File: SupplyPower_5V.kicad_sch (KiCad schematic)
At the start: 3 parts, among them U1 K7805-1000R3

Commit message: Развел все
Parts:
- removed U1: K7805-1000R3, K78xx-1000R3, symbol DCDC_My:K78xx-1000R3
- added D51: +5V, LED_SMD:LED_0805_2012Metric_Pad1.15x1.40mm_HandSolder, symbol Device:LED_Small
- added R97: 500, Resistor_SMD:R_0805_2012Metric_Pad1.20x1.40mm_HandSolder, symbol Device:R_Small
- added U1: K78xxM-1000R3, DCDC_My:K78xxM-1000R3, symbol DCDC_My:K78xxM-1000R3
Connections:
- net +15V: now also U1.1 (Vin)
- net +5V: now also R97.2, U1.3 (+Vo)
- net GND: now also D51.1 (K), U1.2 (GND)
- new net: D51.2 (A), R97.1

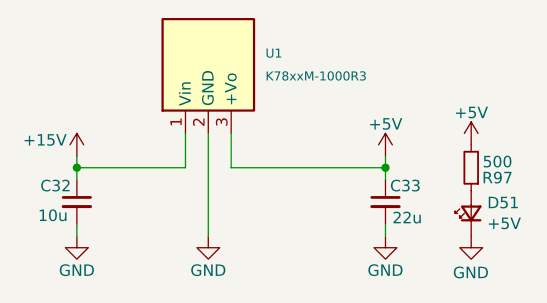
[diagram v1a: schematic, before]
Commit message: Отправил на проверку в резонит: изменил BOM
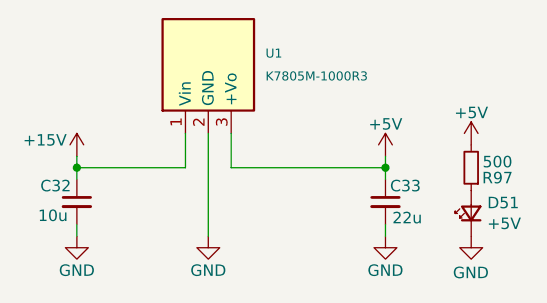
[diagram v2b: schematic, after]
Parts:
- U1: value K78xxM-1000R3 -> K7805M-1000R3
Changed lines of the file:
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@@
 			)
 		)
-		(property "Description" ""
+		(property "Description" "KP-2012SYC"
 			(at 165.1 102.235 0)
 			(effects
@@
 			)
 		)
-		(property "Value" "K78xxM-1000R3"
+		(property "Value" "K7805M-1000R3"
 			(at 142.24 86.995 90)
 			(effects

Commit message: Исправления: исправил нумерацию ножек датчиков тока
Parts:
- U1: footprint DCDC_My:K78xxM-1000R3 -> K78xxM-1000R3
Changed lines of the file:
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@@
 			)
 		)
-		(property "Description" ""
+		(property "Description" "Unpolarized capacitor, small symbol"
 			(at 155.575 100.965 0)
 			(effects
@@
 	)
 	(symbol
-		(lib_name "GND_2")
 		(lib_id "power:GND")
 		(at 121.285 104.775 0)
@@
 			)
 		)
-		(property "Description" ""
+		(property "Description" "Power symbol creates a global label with name \"GND\" , ground"
 			(at 121.285 104.775 0)
 			(effects
@@
 			)
 		)
-		(property "Description" ""
+		(property "Description" "Power symbol creates a global label with name \"GND\" , ground"
 			(at 135.89 104.775 0)
 			(effects
@@
 			)
 		)
-		(property "Description" ""
+		(property "Description" "Unpolarized capacitor, small symbol"
 			(at 121.285 100.965 0)
 			(effects
@@
 			)
 		)
-		(property "Description" ""
+		(property "Description" "Power symbol creates a global label with name \"+15V\""
 			(at 121.285 95.885 0)
 			(effects
@@
 			)
 		)
-		(property "Description" "KP-2012SYC"
+		(property "Description" "Light emitting diode, small symbol"
 			(at 165.1 102.235 0)
 			(effects
@@
 			)
 		)
-		(property "Description" ""
+		(property "Description" "Resistor, small symbol"
 			(at 165.1 97.155 0)
 			(effects
@@
 	)
 	(symbol
-		(lib_name "GND_1")
 		(lib_id "power:GND")
 		(at 155.575 104.775 0)
@@
 			)
 		)
-		(property "Description" ""
+		(property "Description" "Power symbol creates a global label with name \"GND\" , ground"
 			(at 155.575 104.775 0)
 			(effects
@@
 	)
 	(symbol
-		(lib_name "GND_11")
 		(lib_id "power:GND")
 		(at 165.1 104.775 0)
@@
 			)
 		)
-		(property "Description" ""
+		(property "Description" "Power symbol creates a global label with name \"GND\" , ground"
 			(at 165.1 104.775 0)
 			(effects
@@
 			)
 		)
-		(property "Footprint" "DCDC_My:K78xxM-1000R3"
+		(property "Footprint" "K78xxM-1000R3"
 			(at 129.286 85.979 0)
 			(effects

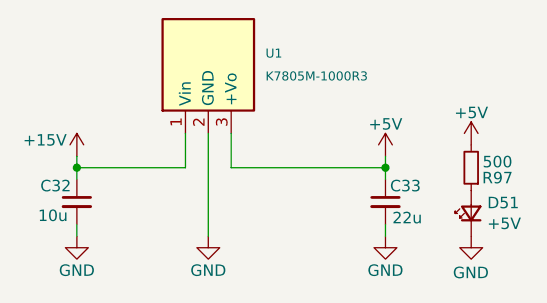
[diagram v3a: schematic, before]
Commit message: Исправления: исправил номиналы подтяжек и сопротивления светодиодов
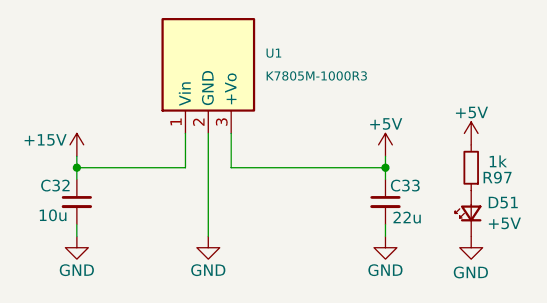
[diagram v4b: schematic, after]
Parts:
- R97: value 500 -> 1k
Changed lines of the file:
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@@
 			)
 		)
-		(property "Value" "500"
+		(property "Value" "1k"
 			(at 168.021 96.52 0)
 			(effects

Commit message: Исправления: заменил полевые на биполярные в контуре RESET и изменил номиналы резисторов базы, исправил BOM
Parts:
- U1: footprint K78xxM-1000R3 -> DCDC_My:K78xxM-1000R3
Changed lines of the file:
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@@
 			)
 		)
-		(property "Footprint" "K78xxM-1000R3"
+		(property "Footprint" "DCDC_My:K78xxM-1000R3"
 			(at 129.286 85.979 0)
 			(effects
